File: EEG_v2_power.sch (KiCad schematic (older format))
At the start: 16 parts, among them J20 BATT_IN+, J21 BATT_IN-, U2 TLV70033, U3 LM2664, U4 TLV70025, U5 TPS72325

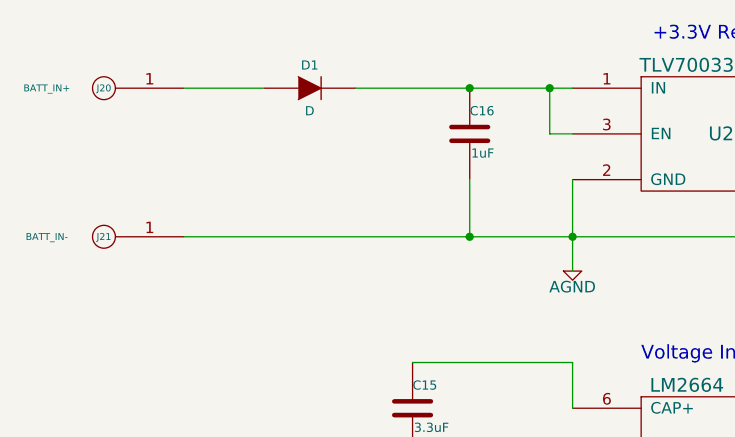
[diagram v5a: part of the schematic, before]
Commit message: Main sheet cleanup
Add pins for raw vin and GND for power switching between USB and
battery.
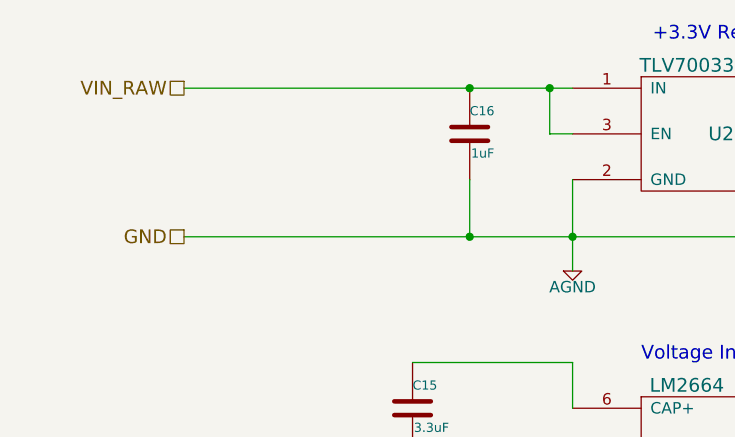
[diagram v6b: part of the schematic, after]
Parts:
- removed D1: D, ~, symbol DIODE
- removed J20: BATT_IN+, ~, symbol SMD_1PIN_PAD
- removed J21: BATT_IN-, ~, symbol SMD_1PIN_PAD
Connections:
- net VIN_RAW: now reaches C16.1, U2.1 (IN), U2.3 (EN)
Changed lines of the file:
@@
 Connection ~ 4550 3050
 Wire Wire Line
-	3700 3050 4650 3050
+	2950 3050 4650 3050
 Connection ~ 4200 3050
 Wire Wire Line
@@
 	6650 4850 6650 5250
 Connection ~ 7050 5250
-$Comp
-L DIODE D1
-U 1 1 54B47FEB
-P 3500 3050
-F 0 "D1" H 3500 3150 40  0000 C CNN
-F 1 "D" H 3500 2950 40  0000 C CNN
-F 2 "~" H 3500 3050 60  0000 C CNN
-F 3 "~" H 3500 3050 60  0000 C CNN
-	1    3500 3050
-	1    0    0    -1
-$EndComp
 Connection ~ 4200 3700
 Wire Wire Line
 	6450 4450 7050 4450
 Connection ~ 6650 4450
-Wire Wire Line
-	3300 3050 2950 3050
 Wire Wire Line
 	5950 3050 7050 3050
@@
 Wire Wire Line
 	6150 4450 6150 4650
-$Comp
-L SMD_1PIN_PAD J20
-U 1 1 54B47FF9
-P 2600 3050
-F 0 "J20" H 2600 3050 30  0000 C CNN
-F 1 "BATT_IN+" H 2850 3050 30  0000 C CNN
-F 2 "~" H 2600 3050 60  0000 C CNN
-F 3 "~" H 2600 3050 60  0000 C CNN
-	1    2600 3050
-	-1   0    0    1
-$EndComp
-$Comp
-L SMD_1PIN_PAD J21
-U 1 1 54B47FFF
-P 2600 3700
-F 0 "J21" H 2600 3700 30  0000 C CNN
-F 1 "BATT_IN-" H 2850 3700 30  0000 C CNN
-F 2 "~" H 2600 3700 60  0000 C CNN
-F 3 "~" H 2600 3700 60  0000 C CNN
-	1    2600 3700
-	-1   0    0    1
-$EndComp
+Text HLabel 2950 3050 0    60   UnSpc ~ 0
+VIN_RAW
+Text HLabel 2950 3700 0    60   UnSpc ~ 0
+GND
 $EndSCHEMATC

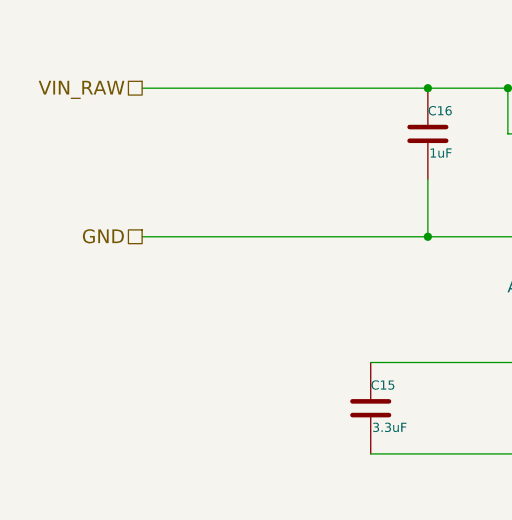
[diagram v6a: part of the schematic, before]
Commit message: Add USB Connector
Added desc of USB A connector
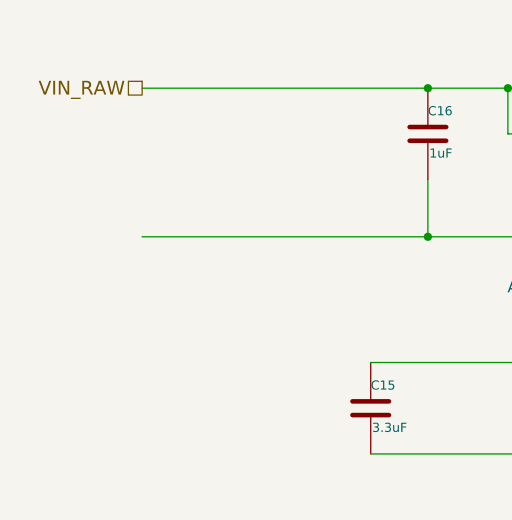
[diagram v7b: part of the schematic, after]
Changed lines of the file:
@@
 LIBS:texas_mod
 LIBS:johanson
+LIBS:conn_mod
 LIBS:EEG_v2-cache
 EELAYER 27 0
@@
 Text HLabel 2950 3050 0    60   UnSpc ~ 0
 VIN_RAW
-Text HLabel 2950 3700 0    60   UnSpc ~ 0
-GND
 $EndSCHEMATC
